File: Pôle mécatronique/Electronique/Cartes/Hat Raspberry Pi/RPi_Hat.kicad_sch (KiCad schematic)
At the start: 7 parts, among them J1 Conn_02x03_Odd_Even, U1 XBee

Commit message: Rangement
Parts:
- added U?: TCAN332G, symbol Interface_CAN_LIN:TCAN332G
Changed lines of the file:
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@@
     (pin "9")
+  )
+  (symbol (lib_id "Interface_CAN_LIN:TCAN332G") (at 100.33 160.02 0) (unit 1)
+    (in_bom yes) (on_board yes) (fields_autoplaced)
+    (property "Reference" "U?" (id 0) (at 102.3494 148.4335 0)
+      (effects (font (size 1.27 1.27)) (justify left))
+    )
+    (property "Value" "TCAN332G" (id 1) (at 102.3494 151.2086 0)
+      (effects (font (size 1.27 1.27)) (justify left))
+    )
+    (property "Footprint" "" (id 2) (at 100.33 172.72 0)
+      (effects (font (size 1.27 1.27) italic) hide)
+    )
+    (property "Datasheet" "http://www.ti.com/lit/ds/symlink/tcan337.pdf" (id 3) (at 100.33 160.02 0)
+      (effects (font (size 1.27 1.27)) hide)
+    )
+    (pin "1")
+    (pin "2")
+    (pin "3")
+    (pin "4")
+    (pin "5")
+    (pin "6")
+    (pin "7")
+    (pin "8")
   )
   (symbol (lib_id "Device:LED") (at 91.44 63.5 0) (unit 1)
@@
       (reference "U?") (unit 1) (value "MCP2515-xSO") (footprint "Package_SO:SOIC-18W_7.5x11.6mm_P1.27mm")
     )
+    (path "/17b65212-5089-4b10-8076-6ae933d78b8b"
+      (reference "U?") (unit 1) (value "TCAN332G") (footprint "")
+    )
   )

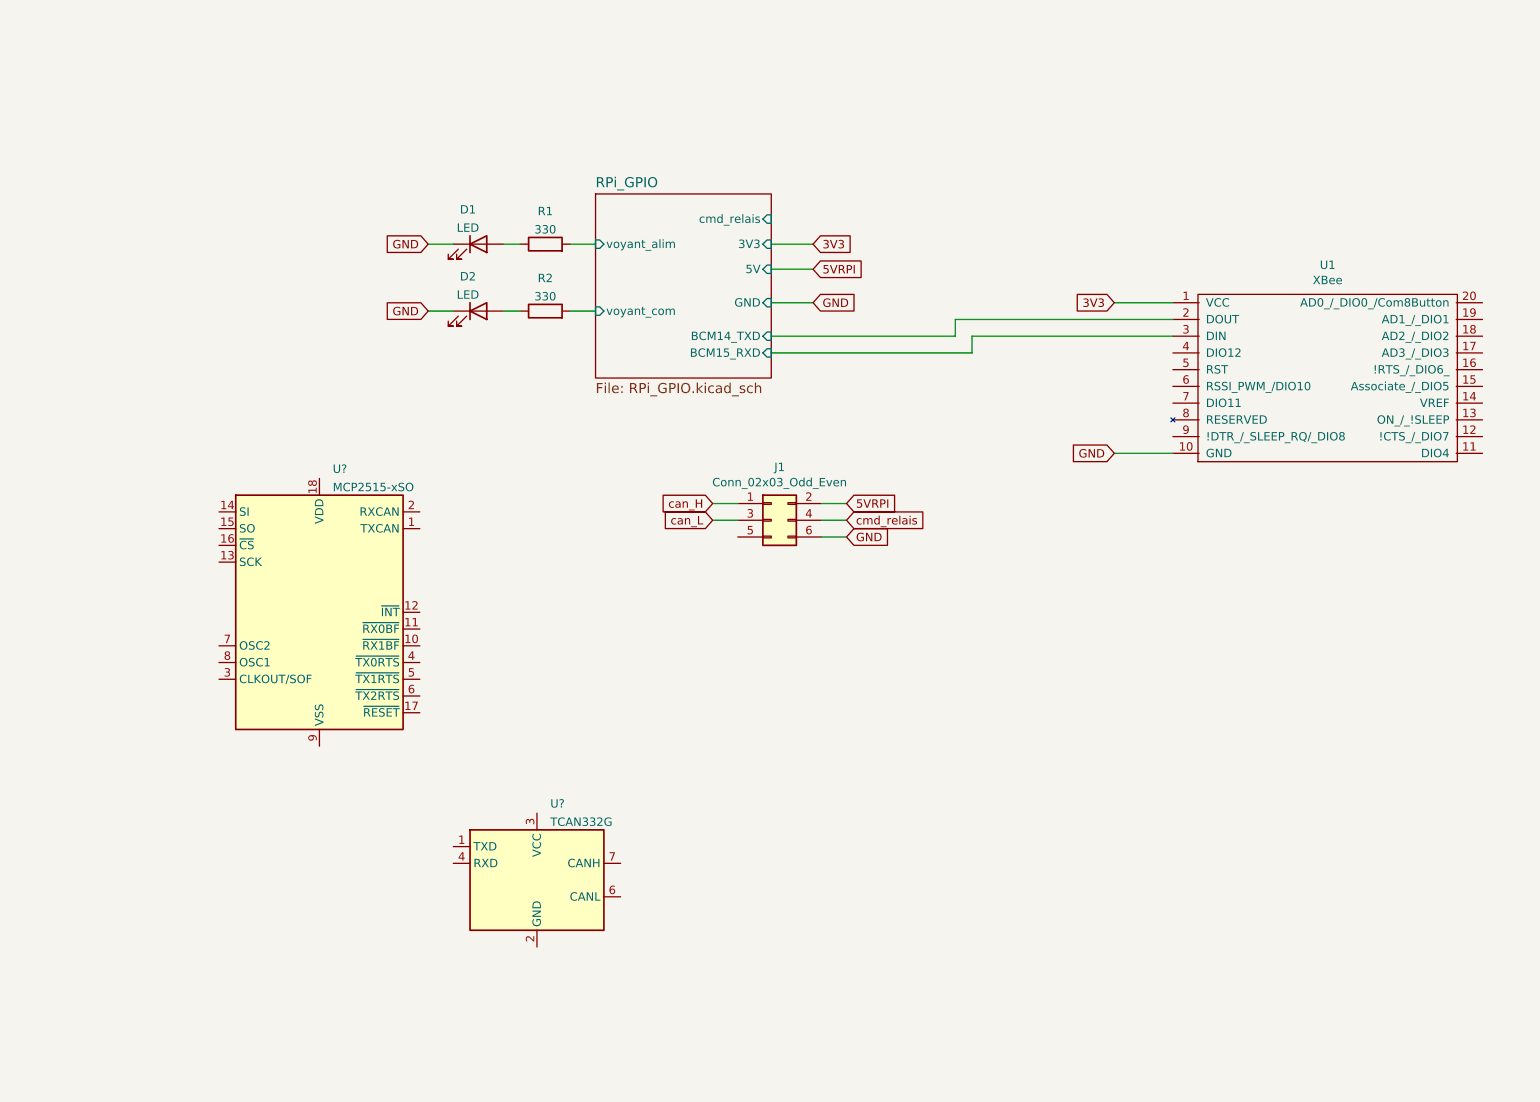
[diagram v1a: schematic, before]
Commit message: Update HAT RPI
- Ajout MCP25625
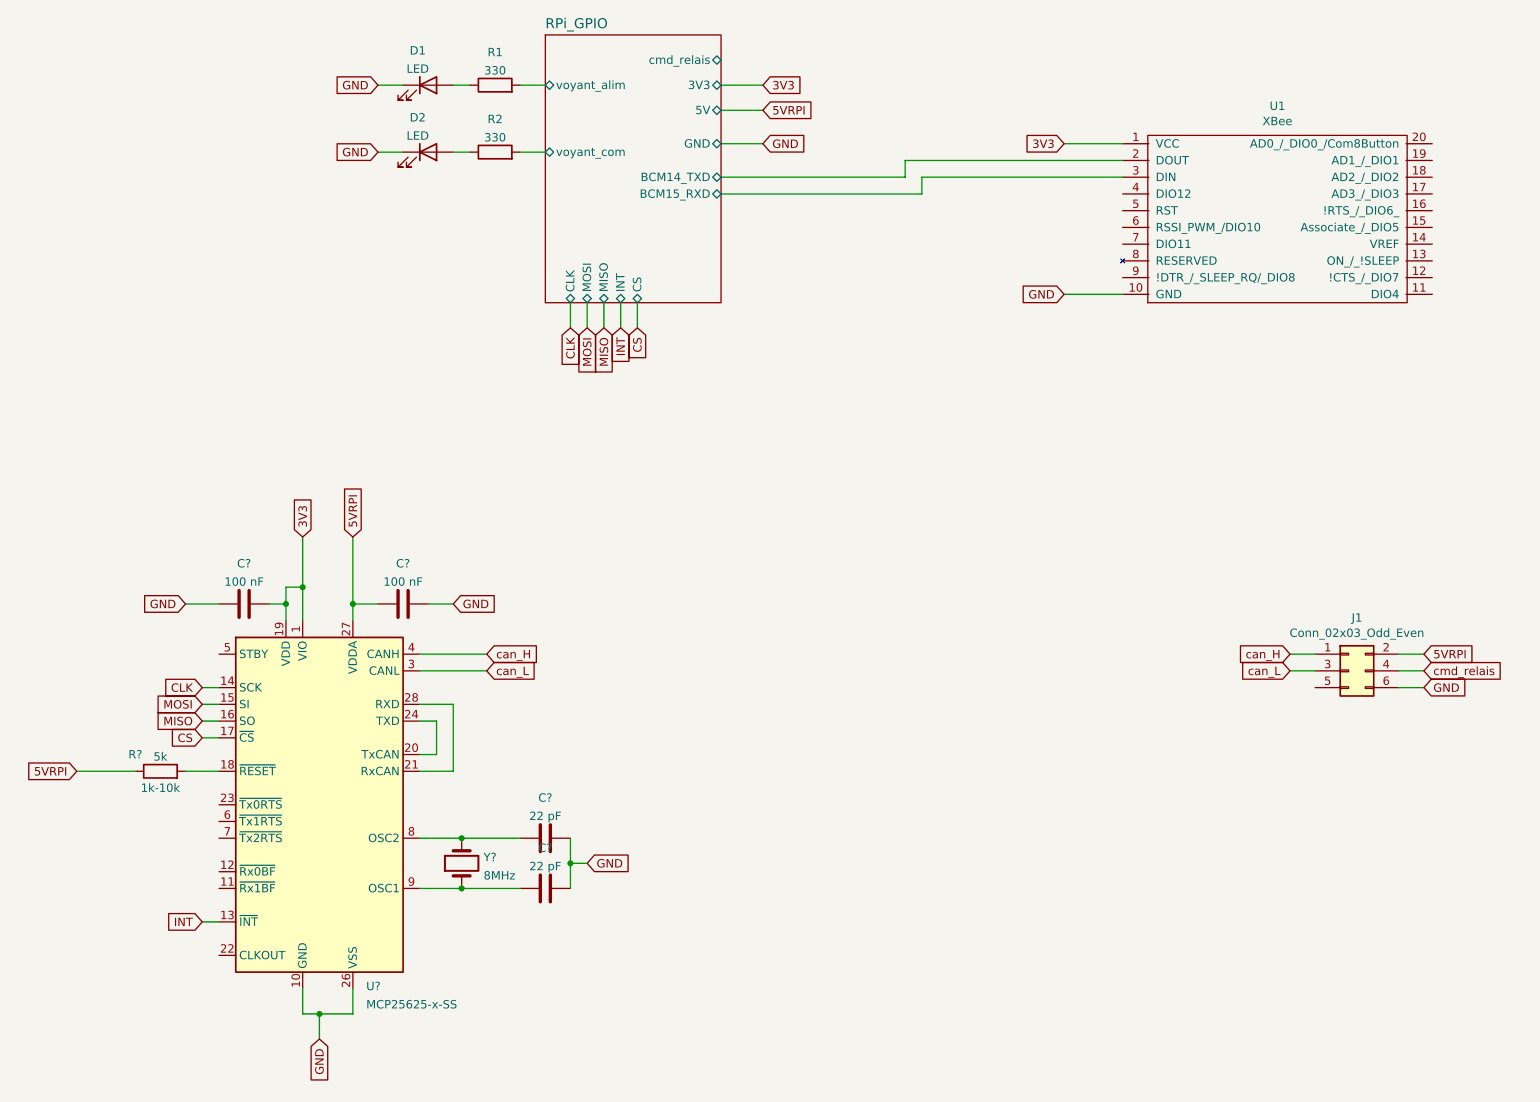
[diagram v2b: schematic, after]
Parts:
- removed U?: MCP2515-xSO, Package_SO:SOIC-18W_7.5x11.6mm_P1.27mm, symbol Interface_CAN_LIN:MCP2515-xSO
- removed U?: TCAN332G, symbol Interface_CAN_LIN:TCAN332G
- added C? (x2): 100 nF, symbol Device:C
- added C? (x2): 22 pF, symbol Device:C
- added R?: 5k, symbol Device:R
- added U?: MCP25625-x-SS, Package_SO:SSOP-28_5.3x10.2mm_P0.65mm, symbol Interface_CAN_LIN:MCP25625-x-SS
- added Y?: 8MHz, symbol Device:Crystal
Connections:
- net 3V3: now also C?.2, U?.1 (VIO), U?.19 (VDD)
- net 5VRPI: now also C?.1, R?.1, U?.27 (VDDA)
- net GND: now also C?.1, C?.2, C?.2, C?.2, U?.10 (GND), U?.26 (VSS)
- net can_H: now also U?.4 (CANH)
- net can_L: now also U?.3 (CANL)
- new net: R?.2, U?.18 (~{RESET})
- new net: C?.1, U?.9 (OSC1), Y?.1
- new net: C?.1, U?.8 (OSC2), Y?.2
- new net: U?.20 (TxCAN), U?.24 (TXD)
- new net: U?.21 (RxCAN), U?.28 (RXD)
- new net CLK: U?.14 (SCK)
- new net CS: U?.17 (~{CS})
- new net INT: U?.13 (~{INT})
- new net MISO: U?.16 (SO)
- new net MOSI: U?.15 (SI)
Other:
- sheet RPi_GPIO ports: added CLK, CS, INT, MISO, MOSI; removed none
- moved on the sheet: D1, D2, J1, R1, R2, U1

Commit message: Update HAT
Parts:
- removed D1, D2: LED, symbol Device:LED
- removed R1, R2: 330, symbol Device:R
- C1, C2, C3, C4: renamed from C?; footprint (none) -> Capacitor_THT:C_Disc_D5.1mm_W3.2mm_P5.00mm
- R3: renamed from R?; footprint (none) -> Resistor_THT:R_Axial_DIN0207_L6.3mm_D2.5mm_P10.16mm_Horizontal
- Y1: renamed from Y?; footprint (none) -> Crystal:Crystal_HC49-U_Vertical
- gave numbers to parts that had none: 1
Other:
- sheet RPi_GPIO ports: added none; removed voyant_alim, voyant_com

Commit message: Update HAT + Commande
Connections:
- net at C4.1, U2.9 (OSC1): now also Y1.2; no longer Y1.1
- net at C3.1, U2.8 (OSC2): now also Y1.1; no longer Y1.2
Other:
- moved on the sheet: Y1
